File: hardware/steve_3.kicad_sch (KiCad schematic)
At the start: 0 parts

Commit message: import BMP388, add BMP388 to pcb and sch
Import BMP388 symbol and footprint to project imports dir. Add BMP388 symbol to schematic and footprint to pcb.
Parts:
- added U4: BMI270, Package_LGA:Bosch_LGA-14_3x2.5mm_P0.5mm, symbol Sensor_Motion:BMI160
- added U5: BMP388, Imported_Footprints:QFN_BMP388_BOS, symbol Imported_Symbols:BMP388
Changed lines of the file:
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@@
 	(generator_version "8.0")
 	(paper "A4")
+	(text_box "NOTE: the following KiCad schematic and footprint are used in this design:\nPackage_LGA:Bosch_LGA-14_3x2.5mm_P0.5mm\nThis package is listed in the KiCad schematic library as being for the BMI160.\nI checked the pin assignments and footprint dimmensions for each sensor and feel comfortable using this schematic/footprint."
+		(exclude_from_sim no)
+		(at 27.94 82.55 0)
+		(size 46.99 17.78)
+		(stroke
+			(width 0)
+			(type default)
+		)
+		(fill
+			(type none)
+		)
+		(effects
+			(font
+				(size 1.27 1.27)
+			)
+			(justify left top)
+		)
+	)
+	(symbol
+		(lib_id "Sensor_Motion:BMI160")
+		(at 54.61 60.96 0)
+		(unit 1)
+		(exclude_from_sim no)
+		(in_bom yes)
+		(on_board yes)
+		(dnp no)
+		(fields_autoplaced yes)
+		(property "Reference" "U4"
+			(at 56.8041 48.26 0)
+			(effects
+				(font
+					(size 1.27 1.27)
+				)
+				(justify left)
+			)
+		)
+		(property "Value" "BMI270"
+			(at 56.8041 50.8 0)
+			(effects
+				(font
+					(size 1.27 1.27)
+				)
+				(justify left)
+			)
+		)
+		(property "Footprint" "Package_LGA:Bosch_LGA-14_3x2.5mm_P0.5mm"
+			(at 54.61 60.96 0)
+			(effects
+				(font
+					(size 1.27 1.27)
+				)
+				(hide yes)
+			)
+		)
+		(property "Datasheet" "https://www.bosch-sensortec.com/media/boschsensortec/downloads/datasheets/bst-bmi270-ds000.pdf"
+			(at 36.83 39.37 0)
+			(effects
+				(font
+					(size 1.27 1.27)
+				)
+				(hide yes)
+			)
+		)
+		(property "Description" "Small, low power inertial measurement unit, LGA-14"
+			(at 54.61 60.96 0)
+			(effects
+				(font
+					(size 1.27 1.27)
+				)
+				(hide yes)
+			)
+		)
+		(pin "10"
+		)
+		(pin "1"
+		)
+		(pin "11"
+		)
+		(pin "3"
+		)
+		(pin "2"
+		)
+		(pin "13"
+		)
+		(pin "6"
+		)
+		(pin "7"
+		)
+		(pin "9"
+		)
+		(pin "12"
+		)
+		(pin "4"
+		)
+		(pin "5"
+		)
+		(pin "8"
+		)
+		(pin "14"
+		)
+		(instances
+			(project ""
+				(path "/f7ed98e3-ddd9-4c0c-9e06-df5f86e74283/203efb9b-0e38-445a-a51a-cbb7d642002b"
+					(reference "U4")
+					(unit 1)
+				)
+			)
+		)
+	)
+	(symbol
+		(lib_id "Imported_Symbols:BMP388")
+		(at 90.17 48.26 0)
+		(unit 1)
+		(exclude_from_sim no)
+		(in_bom yes)
+		(on_board yes)
+		(dnp no)
+		(property "Reference" "U5"
+			(at 110.49 36.576 0)
+			(effects
+				(font
+					(size 1.524 1.524)
+				)
+				(justify left)
+			)
+		)
+		(property "Value" "BMP388"
+			(at 106.934 40.894 0)
+			(effects
+				(font
+					(size 1.524 1.524)
+				)
+				(justify left)
+			)
+		)
+		(property "Footprint" "Imported_Footprints:QFN_BMP388_BOS"
+			(at 88.138 44.45 0)
+			(effects
+				(font
+					(size 1.27 1.27)
+					(italic yes)
+				)
+				(hide yes)
+			)
+		)
+		(property "Datasheet" "BMP388"
+			(at 102.362 44.704 0)
+			(effects
+				(font
+					(size 1.27 1.27)
+					(italic yes)
+				)
+				(hide yes)
+			)
+		)
+		(property "Description" ""
+			(at 90.17 48.26 0)
+			(effects
+				(font
+					(size 1.27 1.27)
+				)
+				(hide yes)
+			)
+		)
+		(pin "3"
+		)
+		(pin "5"
+		)
+		(pin "1"
+		)
+		(pin "2"
+		)
+		(pin "10"
+		)
+		(pin "4"
+		)
+		(pin "6"
+		)
+		(pin "7"
+		)
+		(pin "9"
+		)
+		(pin "8"
+		)
+		(instances
+			(project ""
+				(path "/f7ed98e3-ddd9-4c0c-9e06-df5f86e74283/203efb9b-0e38-445a-a51a-cbb7d642002b"
+					(reference "U5")
+					(unit 1)
+				)
+			)
+		)
+	)
 )

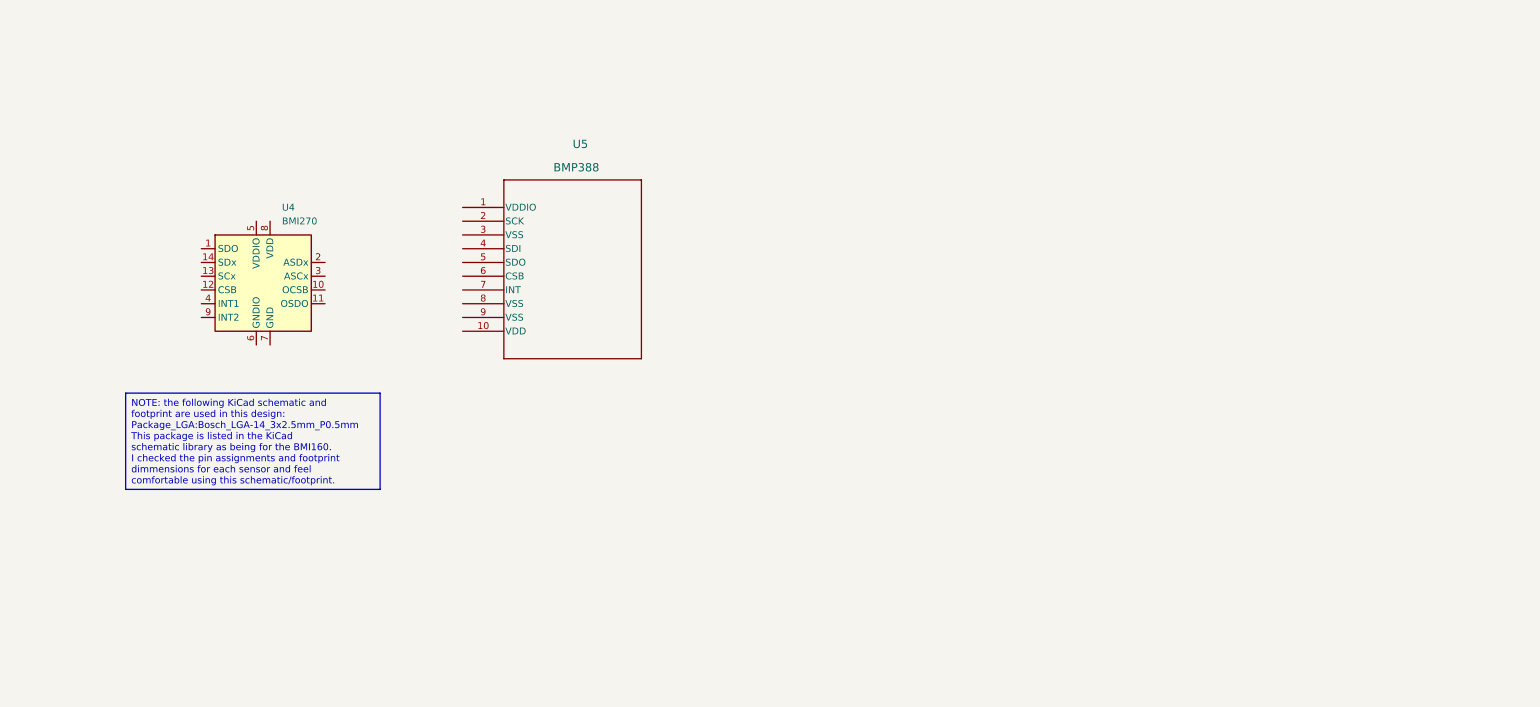
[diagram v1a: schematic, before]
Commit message: Finished sensor, flash, and SD card in schematic; Updated README for remaining items
Finished BMI270 and BMP390, Flash storage, and  microSD card in schematic; Updated README for remaining items
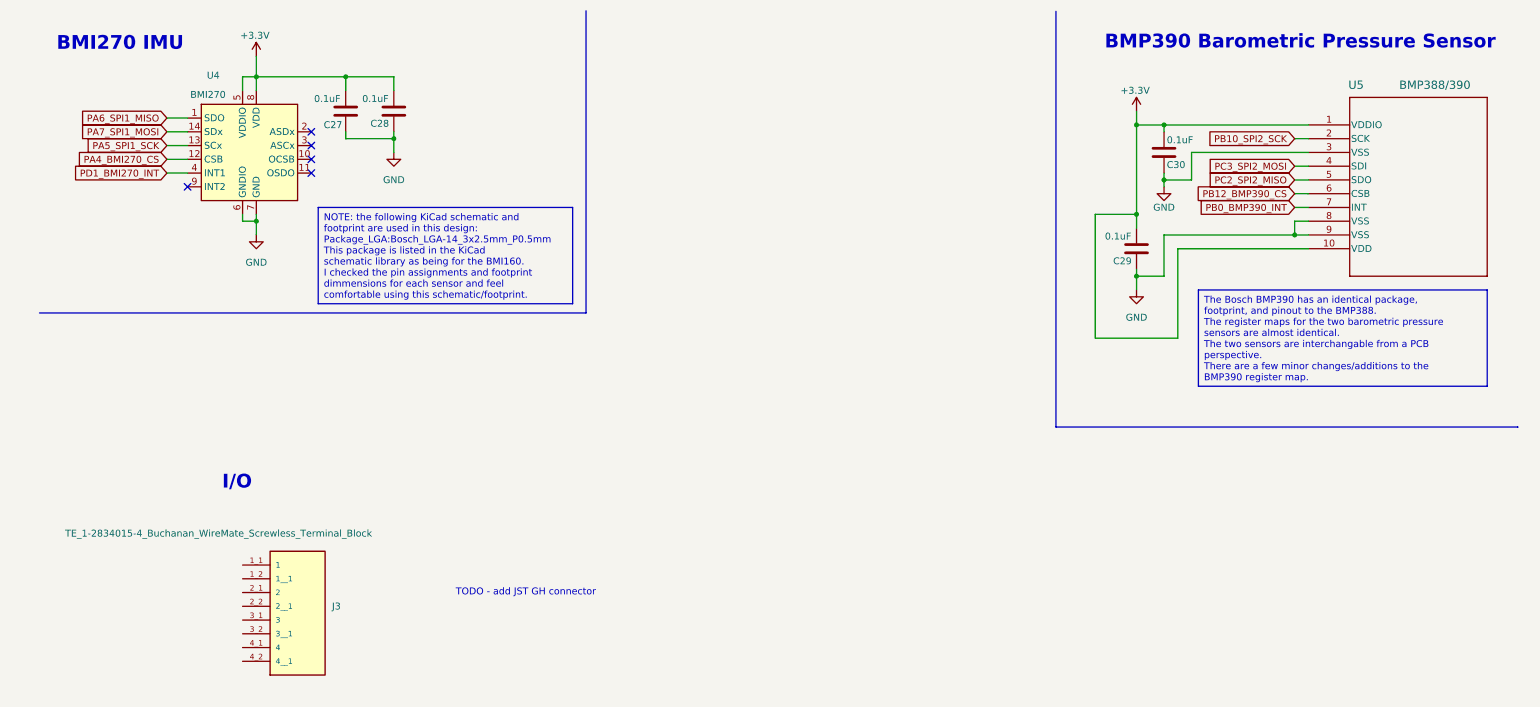
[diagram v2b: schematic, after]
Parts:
- added C27, C28, C29, C30: 0.1uF, Capacitor_SMD:C_0603_1608Metric, symbol Device:C
- added J3: TE_1-2834015-4_Buchanan_WireMate_Screwless_Termin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, Imported_Footprints:TE_1-2834015-4_Buchanan_WireMate_Screwless_Terminal_Block, symbol Imported_Symbols:TE_1-2834015-4_Buchanan_WireMate_Screwless_Terminal_Block
- U5: value BMP388 -> BMP388/390
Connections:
- net PA6_SPI1_MISO: now reaches U4.1 (SDO)
- net PA4_BMI270_CS: now reaches U4.12 (CSB)
- net PA5_SPI1_SCK: now reaches U4.13 (SCx)
- net PA7_SPI1_MOSI: now reaches U4.14 (SDx)
- net PD1_BMI270_INT: now reaches U4.4 (INT1)
- net +3.3V: now reaches U4.5 (VDDIO)
- net +3.3V: now also U4.8 (VDD), U5.1 (VDDIO), U5.10 (VDD), C27.1, C28.1, C29.1, C30.1
- net GND: now reaches U4.6 (GNDIO)
- net GND: now also U4.7 (GND), U5.3 (VSS), U5.8 (VSS), U5.9 (VSS), C27.2, C28.2, C29.2, C30.2
- net PB10_SPI2_SCK: now reaches U5.2 (SCK)
- net PC3_SPI2_MOSI: now reaches U5.4 (SDI)
- net PC2_SPI2_MISO: now reaches U5.5 (SDO)
- net PB12_BMP390_CS: now reaches U5.6 (CSB)
- net PB0_BMP390_INT: now reaches U5.7 (INT)
- no-connect marks 0 -> 5
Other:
- note added: "BMI270 IMU"
- note added: "BMP390 Barometric Pressure Sensor"
- note added: "I/O"
- note added: "TODO - add JST GH connector"
- moved on the sheet: U4, U5

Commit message: Add components to schematic; fix existing ones
Added additional components to schematic such as IO connectors. Replaced the 10A TO-263-2 diode rectifiers with much smaller 5A ones.
Other various fixes.
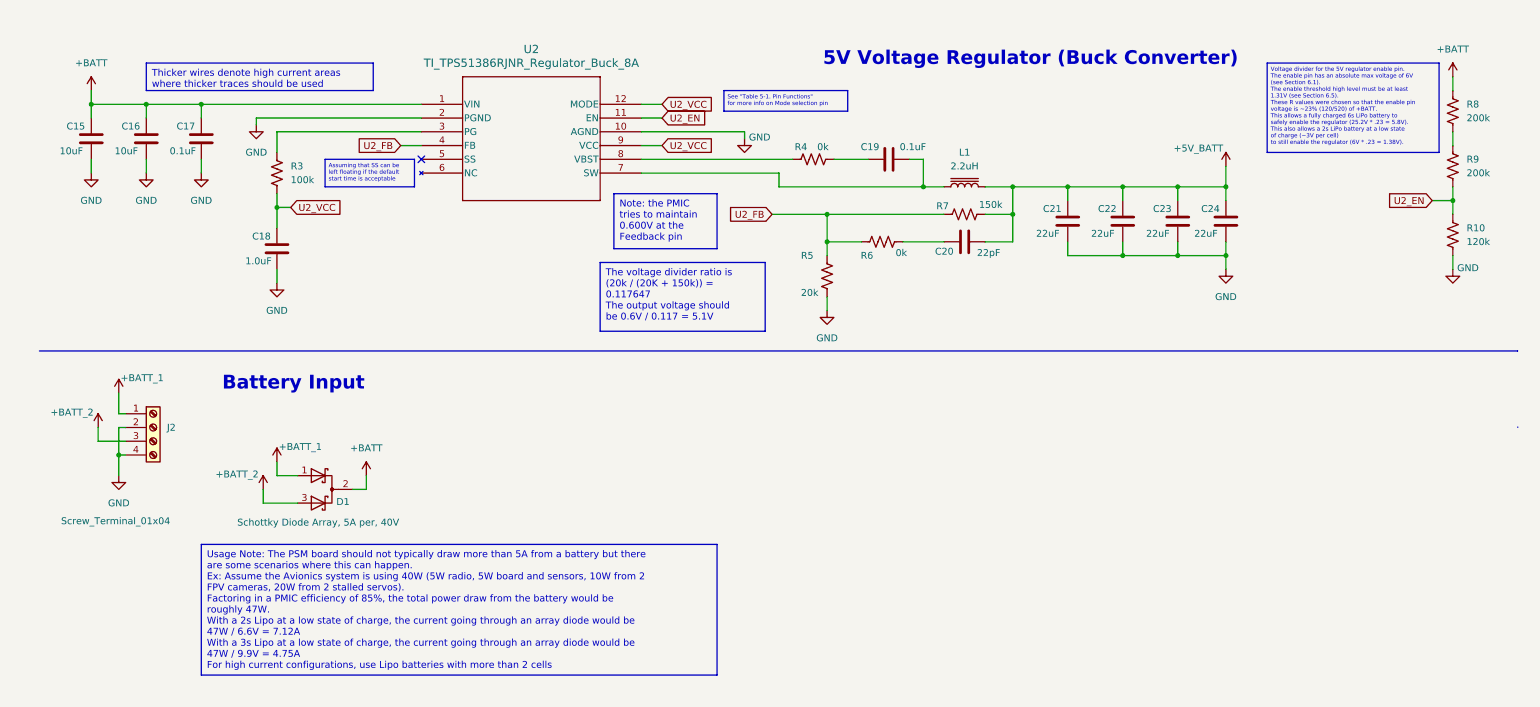
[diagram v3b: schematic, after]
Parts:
- removed C27, C28, C29, C30: 0.1uF, Capacitor_SMD:C_0603_1608Metric, symbol Device:C
- removed J3: TE_1-2834015-4_Buchanan_WireMate_Screwless_Termin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, Imported_Footprints:TE_1-2834015-4_Buchanan_WireMate_Screwless_Terminal_Block, symbol Imported_Symbols:TE_1-2834015-4_Buchanan_WireMate_Screwless_Terminal_Block
- removed U4: BMI270, Package_LGA:Bosch_LGA-14_3x2.5mm_P0.5mm, symbol Sensor_Motion:BMI160
- removed U5: BMP388/390, Imported_Footprints:QFN_BMP388_BOS, symbol Imported_Symbols:BMP388
- added C15, C16: 10uF, Capacitor_SMD:C_1206_3216Metric, symbol Device:C
- added C17, C19: 0.1uF, Capacitor_SMD:C_0603_1608Metric, symbol Device:C
- added C18: 1.0uF, Capacitor_SMD:C_0603_1608Metric, symbol Device:C
- added C20: 22pF, Capacitor_SMD:C_0603_1608Metric, symbol Device:C
- added C21, C22, C23, C24: 22uF, Capacitor_SMD:C_1206_3216Metric, symbol Device:C
- added D1: Schottky Diode Array, 5A per, 40V, Imported_Footprints:PDS1040CTL-13_PowerDI-5, symbol Device:D_Schottky_Dual_CommonCathode_AKA_Parallel
- added J2: Screw_Terminal_01x04, TerminalBlock_Phoenix:TerminalBlock_Phoenix_PT-1,5-4-5.0-H_1x04_P5.00mm_Horizontal, symbol Connector:Screw_Terminal_01x04
- added L1: 2.2uH, Inductor_SMD:L_Coilcraft_XAL6060-XXX, symbol Device:L_Iron
- added R10: 120k, Resistor_SMD:R_0603_1608Metric, symbol Device:R_US
- added R3: 100k, Resistor_SMD:R_0603_1608Metric, symbol Device:R_US
- added R4, R6: 0k, Resistor_SMD:R_0603_1608Metric, symbol Device:R_US
- added R5: 20k, Resistor_SMD:R_0603_1608Metric, symbol Device:R_US
- added R7: 150k, Resistor_SMD:R_0603_1608Metric, symbol Device:R_US
- added R8, R9: 200k, Resistor_SMD:R_0603_1608Metric, symbol Device:R_US
- added U2: TI_TPS51386RJNR_Regulator_Buck_8A, Imported_Footprints:TI_TPS51386RJNR_VQFN-HR_REG_BUCK_8A, symbol Imported_Symbols:TI_TPS51386RJNR_Regulator_Buck_8A
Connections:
- net GND: now also C15.2, C16.2, C17.2, C18.2, C21.2, C22.2, C23.2, C24.2, J2.2 (Pin_2), J2.4 (Pin_4), R10.2, R5.1, U2.10 (AGND), U2.2 (PGND)
- new net: C19.1, R4.2
- new net: C19.2, L1.1, U2.7 (SW)
- new net: R4.1, U2.8 (VBST)
- new net: R8.2, R9.1
- new net: R3.1, U2.3 (PG)
- new net: C20.1, R6.2
- new net +5V_BATT: C20.2, C21.1, C22.1, C23.1, C24.1, L1.2, R7.2
- new net +BATT: C15.1, C16.1, C17.1, D1.2 (K), R8.1, U2.1 (VIN)
- new net +BATT_1: D1.1 (A), J2.1 (Pin_1)
- new net +BATT_2: D1.3 (A), J2.3 (Pin_3)
- new net U2_EN: R10.1, R9.2, U2.11 (EN)
- new net U2_FB: R5.2, R6.1, R7.1, U2.4 (FB)
- new net U2_VCC: C18.1, R3.2, U2.12 (MODE), U2.9 (VCC)
- no-connect marks 5 -> 1
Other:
- note added: "5V Voltage Regulator (Buck Converter)"
- note added: "Battery Input"
- note removed: "BMI270 IMU"
- note removed: "BMP390 Barometric Pressure Sensor"
- note removed: "I/O"
- note removed: "TODO - add JST GH connector"
